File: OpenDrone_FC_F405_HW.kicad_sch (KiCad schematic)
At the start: 106 parts, among them J1 Conn_01x05, J10 Conn_01x02, J12 Conn_01x02, J13 Conn_01x02, J14 Conn_01x02, J15 Conn_01x02, J16 Conn_01x02, J17 Conn_01x02, J19 Conn_01x02, J2 Conn_01x02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

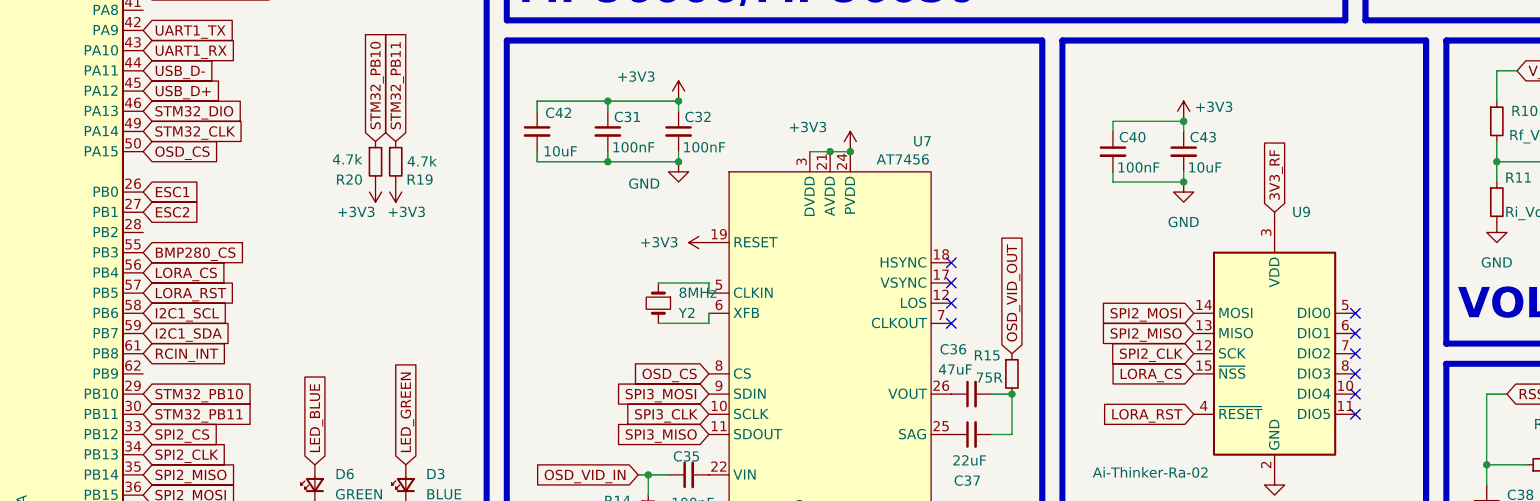
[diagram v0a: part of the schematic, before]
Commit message: add LoRa IRQ
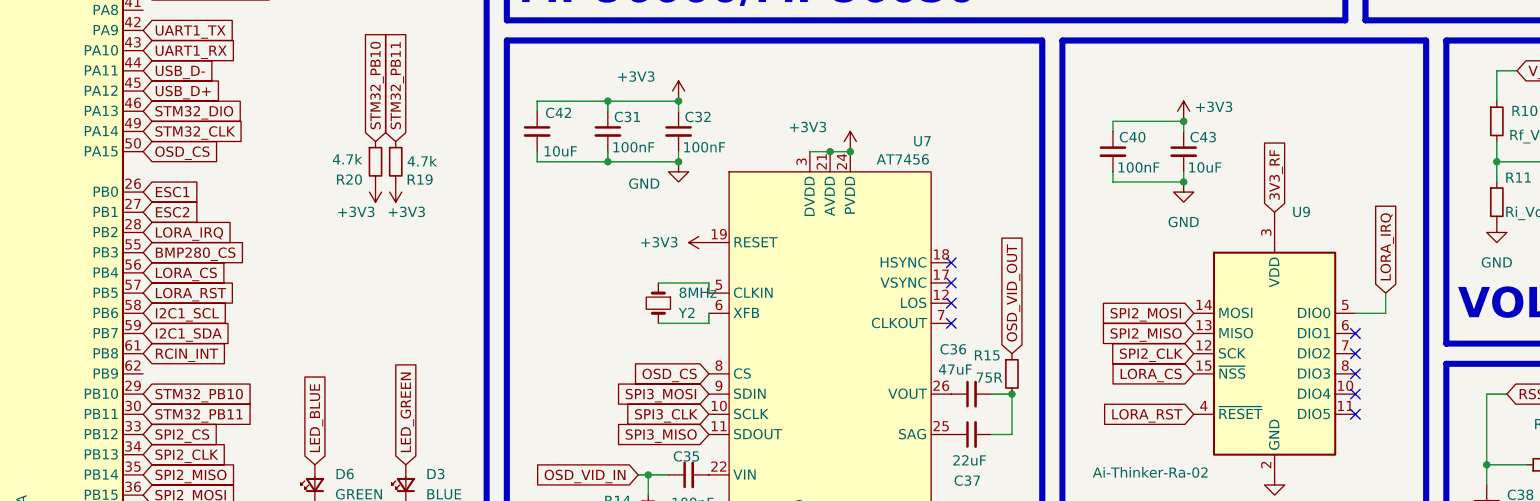
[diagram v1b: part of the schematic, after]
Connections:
- net LORA_IRQ: now reaches U9.5 (DIO0)
- net LORA_IRQ: now also U1.28 (PB2)
- no-connect marks 14 -> 13

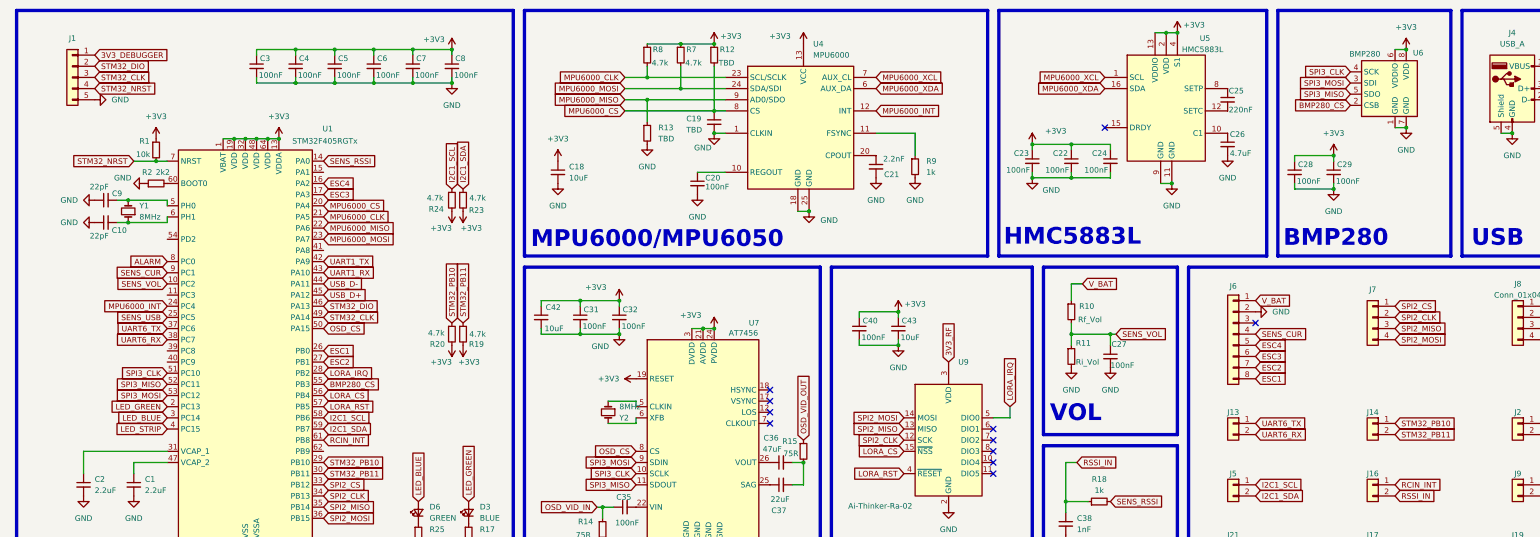
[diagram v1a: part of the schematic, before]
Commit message: use mpu6050 and change spi pinout
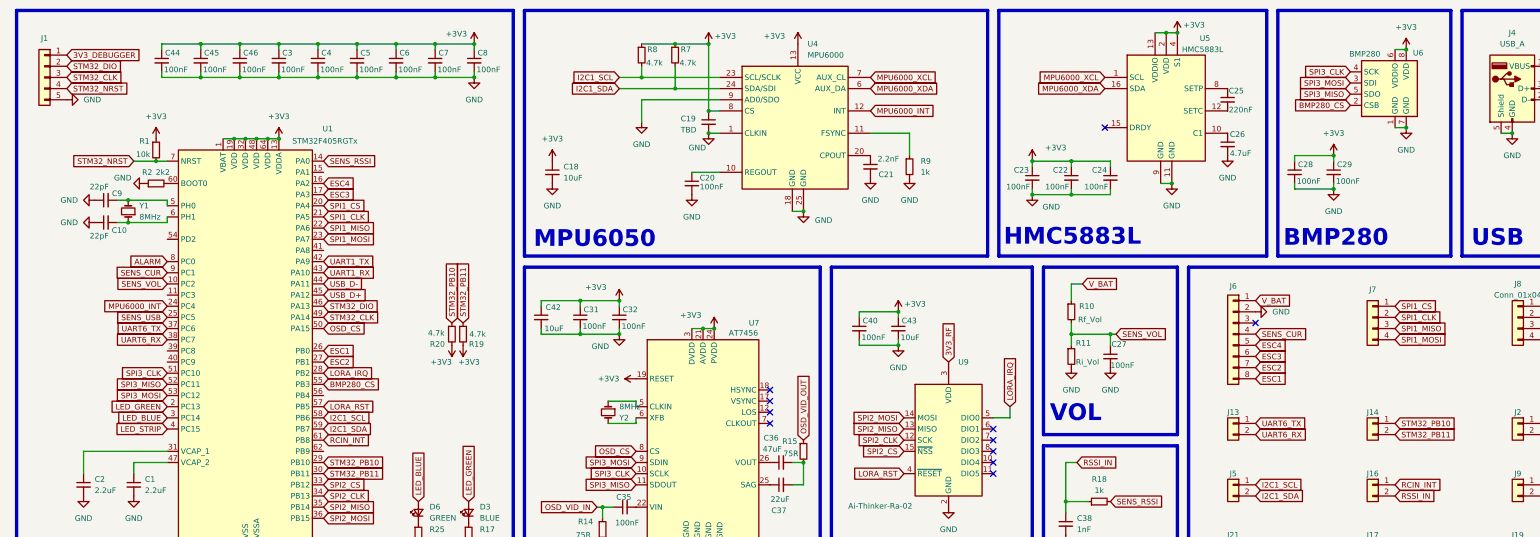
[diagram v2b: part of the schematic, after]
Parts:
- removed R12, R13: TBD, Capacitor_SMD:C_0402_1005Metric, symbol Device:R_Small
- removed R23, R24: 4.7k, Resistor_SMD:R_0402_1005Metric, symbol Device:R_Small
- added C44, C45, C46: 100nF, Capacitor_SMD:C_0402_1005Metric, symbol Device:C_Small
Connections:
- net +3V3: now also C19.1, U4.8 (CS), C44.1, C45.1, C46.1
- net GND: now also U4.9 (AD0/SDO), C44.2, C45.2, C46.2
- net I2C1_SCL: now also R8.2, U4.23 (SCL/SCLK)
- net I2C1_SDA: now also R7.2, U4.24 (SDA/SDI)
- net SPI2_CLK: no longer J7.2 (Pin_2)
- net SPI2_CS: now also U9.15 (~{NSS}); no longer J7.1 (Pin_1)
- net SPI2_MISO: no longer J7.3 (Pin_3)
- net SPI2_MOSI: no longer J7.4 (Pin_4)
- net LORA_CS: no longer names the net of U1.56 (PB4)
- net LORA_CS: no longer U9.15 (~{NSS})
- removed net MPU6000_CLK: R8.2, U1.21 (PA5), U4.23 (SCL/SCLK)
- removed net MPU6000_CS: C19.1, U1.20 (PA4), U4.8 (CS)
- net MPU6000_MISO renamed SPI1_MISO
- net SPI1_MISO: now also J7.3 (Pin_3); no longer U4.9 (AD0/SDO)
- removed net MPU6000_MOSI: R7.2, U1.23 (PA7), U4.24 (SDA/SDI)
- new net SPI1_CLK: J7.2 (Pin_2), U1.21 (PA5)
- new net SPI1_CS: J7.1 (Pin_1), U1.20 (PA4)
- new net SPI1_MOSI: J7.4 (Pin_4), U1.23 (PA7)
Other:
- note added: "MPU6050"
- note removed: "MPU6000/MPU6050"
- moved on the sheet: C18, C19, C20, C21, C22, C23, C24, C3, C4, C5, C6, C7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

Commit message: update project
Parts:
- removed C30, C34, C42: 10uF, Capacitor_SMD:C_1210_3225Metric, symbol Device:C_Small
- removed C31, C32, C35: 100nF, Capacitor_SMD:C_0402_1005Metric, symbol Device:C_Small
- removed C33, C40, C41: 100nF, Capacitor_SMD:C_1210_3225Metric, symbol Device:C_Small
- removed C36: 47uF, Capacitor_SMD:C_0402_1005Metric, symbol Device:C_Small
- removed C37: 22uF, Capacitor_SMD:C_0402_1005Metric, symbol Device:C_Small
- removed C38: 1nF, Capacitor_SMD:C_0402_1005Metric, symbol Device:C_Small
- removed C43: 10uF, Capacitor_SMD:C_0805_2012Metric, symbol Device:C_Small
- removed D5: SS34, Diode_SMD:D_SMA, symbol Device:D_Schottky
- removed J12, J15, J16, J17, J19, J20, J21: Conn_01x02, Footprint:MountingPad_1x2, symbol Connector_Generic:Conn_01x02
- removed J4: USB_A, Footprint:USB_Micro-B_SMD, symbol Connector:USB_A
- removed J7: Conn_01x04, Footprint:MountingPad_1x4, symbol Connector_Generic:Conn_01x04
- removed R14, R15: 75R, Resistor_SMD:R_0402_1005Metric, symbol Device:R_Small
- removed R18: 1k, Resistor_SMD:R_0402_1005Metric, symbol Device:R_Small
- removed R4, R6: 10k, Resistor_SMD:R_0402_1005Metric, symbol Device:R_Small
- removed U7: AT7456, Package_SO:TSSOP-28-1EP_4.4x9.7mm_P0.65mm, symbol AT7456:AT7456
- removed U9: Ai-Thinker-Ra-02, Footprint:Ai-Thinker-Ra-02-LoRa, symbol RF_Module:Ai-Thinker-Ra-02
- removed Y2: 8MHz, Crystal:Crystal_SMD_3225-4Pin_3.2x2.5mm, symbol Device:Crystal_Small
- added J11, J12, J16: Conn_01x05, Connector_PinHeader_2.00mm:PinHeader_1x05_P2.00mm_Vertical, symbol Connector_Generic:Conn_01x05
- added J3, J4, J7: Conn_01x02, Footprint:HolePad_1x2, symbol Connector_Generic:Conn_01x02
- C19: value TBD -> 10nF
- J13, J14, J2, J5, J9: footprint Footprint:MountingPad_1x2 -> Footprint:HolePad_1x2
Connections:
- net OSD_VID_IN is gone; now on net +5V: J2.1 (Pin_1)
- net OSD_VID_OUT is gone; now on net GND: J2.2 (Pin_2)
- net +3V3: now also J14.1 (Pin_1), J16.5 (Pin_5), J3.1 (Pin_1), J4.1 (Pin_1)
- net +5V: now also J13.1 (Pin_1), J16.3 (Pin_3)
- net ALARM: now also J9.2 (Pin_2); no longer J9.1 (Pin_1)
- net GND: now also J13.2 (Pin_2), J14.2 (Pin_2), J16.4 (Pin_4), J3.2 (Pin_2), J4.2 (Pin_2)
- net I2C1_SCL: now also U6.4 (SCK)
- net I2C1_SDA: now also U6.3 (SDI)
- net LED_STRIP: now also J9.1 (Pin_1); no longer J9.2 (Pin_2)
- net LORA_IRQ: now also J12.5 (Pin_5)
- net LORA_RST: now also J11.5 (Pin_5)
- net OSD_CS: no longer U1.50 (PA15)
- net SPI1_CLK: now also J11.2 (Pin_2)
- net SPI1_CS: now also J11.1 (Pin_1)
- net SPI1_MISO: now also J11.3 (Pin_3)
- net SPI1_MOSI: now also J11.4 (Pin_4)
- net SPI2_CLK: now also J12.2 (Pin_2)
- net SPI2_CS: now also J12.1 (Pin_1)
- net SPI2_MISO: now also J12.3 (Pin_3)
- net SPI2_MOSI: now also J12.4 (Pin_4)
- net STM32_PB10: now also J16.1 (Pin_1); no longer J14.1 (Pin_1)
- net STM32_PB11: now also J16.2 (Pin_2); no longer J14.2 (Pin_2)
- net UART6_RX: now also J7.2 (Pin_2); no longer J13.2 (Pin_2)
- net UART6_TX: now also J7.1 (Pin_1); no longer J13.1 (Pin_1)
- net BMP280_CS: no longer names the net of U6.2 (CSB)
- net BMP280_CS: no longer U1.55 (PB3)
- net RCIN_INT: no longer names the net of U1.61 (PB8)
- net SENS_RSSI: no longer names the net of U1.14 (PA0)
- net SENS_USB: no longer names the net of U1.25 (PC5)
- net SPI3_CLK: no longer names the net of U1.51 (PC10)
- net SPI3_CLK: no longer U6.4 (SCK)
- net SPI3_MISO: no longer names the net of U6.5 (SDO)
- net SPI3_MISO: no longer U1.52 (PC11)
- net SPI3_MOSI: no longer names the net of U1.53 (PC12)
- net SPI3_MOSI: no longer U6.3 (SDI)
- net USB_D+: no longer names the net of U1.45 (PA12)
- net USB_D-: no longer names the net of U1.44 (PA11)
- no-connect marks 13 -> 6
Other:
- note removed: "LORA"
- note removed: "OSD"
- note removed: "RSSI"
- note removed: "USB"
- moved on the sheet: C14, C15, C16, C17, C27, C28, C29, C39, D2, D3, D4, D6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

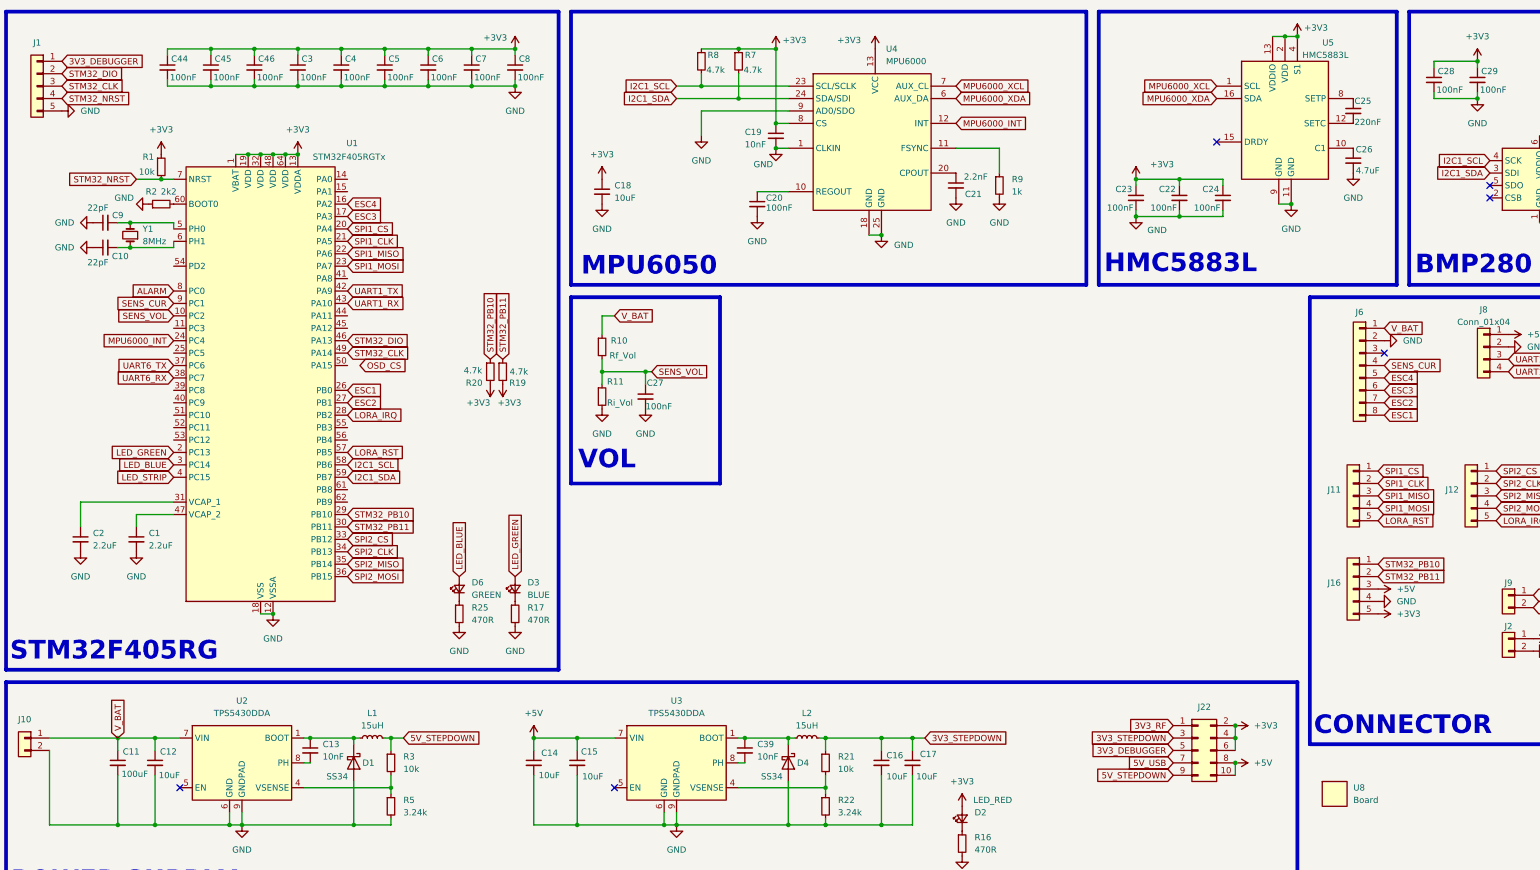
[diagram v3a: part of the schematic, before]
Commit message: update placement
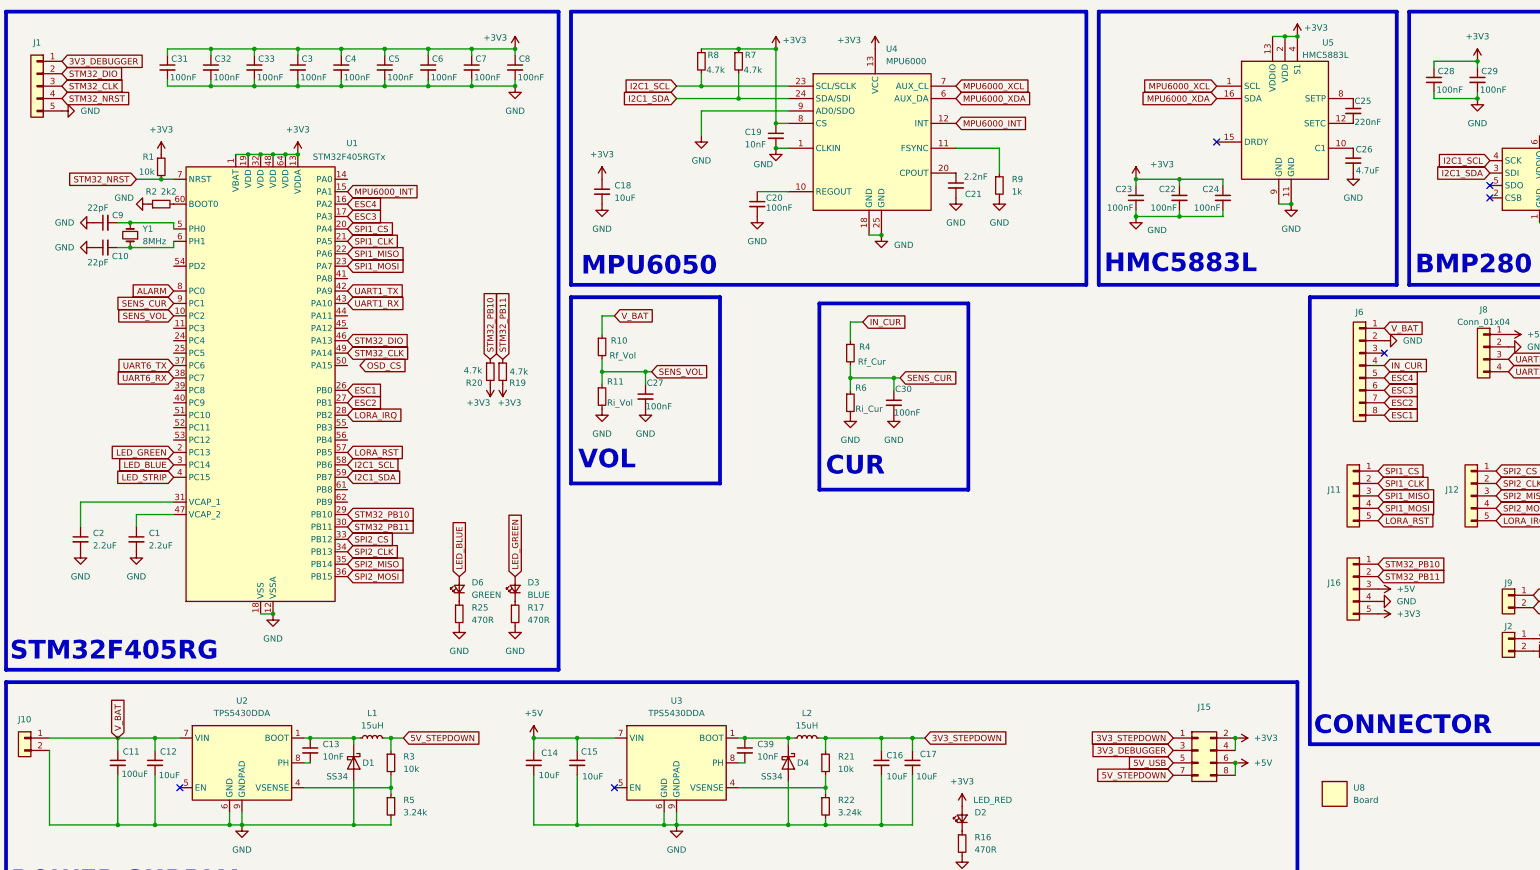
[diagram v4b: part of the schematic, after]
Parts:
- removed C44, C45, C46: 100nF, Capacitor_SMD:C_0402_1005Metric, symbol Device:C_Small
- removed J22: Conn_02x05_Odd_Even, Connector_PinHeader_1.27mm:PinHeader_2x05_P1.27mm_Vertical, symbol Connector_Generic:Conn_02x05_Odd_Even
- added C30, C31, C32, C33: 100nF, Capacitor_SMD:C_0402_1005Metric, symbol Device:C_Small
- added J15: Conn_02x04_Odd_Even, Connector_PinHeader_1.27mm:PinHeader_2x04_P1.27mm_Vertical, symbol Connector_Generic:Conn_02x04_Odd_Even
- added R4: Rf_Cur, Resistor_SMD:R_0402_1005Metric, symbol Device:R_Small
- added R6: Ri_Cur, Resistor_SMD:R_0402_1005Metric, symbol Device:R_Small
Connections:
- net +3V3: now also C31.1, C32.1, C33.1, J15.2 (Pin_2), J15.4 (Pin_4)
- net +5V: now also J15.6 (Pin_6), J15.8 (Pin_8)
- net 3V3_DEBUGGER: now also J15.3 (Pin_3)
- net 3V3_STEPDOWN: now also J15.1 (Pin_1)
- net 5V_STEPDOWN: now also J15.7 (Pin_7)
- net 5V_USB: now also J15.5 (Pin_5)
- net GND: now also C30.2, C31.2, C32.2, C33.2, R6.2
- net MPU6000_INT: now also U1.15 (PA1); no longer U1.24 (PC4)
- net SENS_CUR: now also C30.1, R4.2, R6.1; no longer J6.4 (Pin_4)
- new net IN_CUR: J6.4 (Pin_4), R4.1
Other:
- note added: "CUR"

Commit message: update project
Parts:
- removed J15: Conn_02x04_Odd_Even, Connector_PinHeader_1.27mm:PinHeader_2x04_P1.27mm_Vertical, symbol Connector_Generic:Conn_02x04_Odd_Even
- added J17: Conn_02x03_Odd_Even, Connector_PinHeader_1.27mm:PinHeader_2x03_P1.27mm_Vertical, symbol Connector_Generic:Conn_02x03_Odd_Even
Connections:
- net +3V3: now also J17.2 (Pin_2), J17.4 (Pin_4)
- net +5V: now also J17.5 (Pin_5)
- net 3V3_DEBUGGER: now also J17.3 (Pin_3)
- net 3V3_STEPDOWN: now also J17.1 (Pin_1)
- net 5V_STEPDOWN: now also J17.6 (Pin_6)
- net LORA_IRQ: now also J11.1 (Pin_1), U1.45 (PA12); no longer J12.5 (Pin_5), U1.28 (PB2)
- net LORA_RST: now also J12.1 (Pin_1), U1.44 (PA11); no longer J11.5 (Pin_5), U1.57 (PB5)
- net SPI1_CLK: no longer J11.2 (Pin_2)
- net SPI1_CS: no longer J11.1 (Pin_1)
- net SPI1_MISO: no longer J11.3 (Pin_3)
- net SPI1_MOSI: no longer J11.4 (Pin_4)
- net SPI2_CLK: now also J11.4 (Pin_4); no longer J12.2 (Pin_2)
- net SPI2_CS: now also J11.5 (Pin_5); no longer J12.1 (Pin_1)
- net SPI2_MISO: now also J11.3 (Pin_3); no longer J12.3 (Pin_3)
- net SPI2_MOSI: now also J11.2 (Pin_2); no longer J12.4 (Pin_4)
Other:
- moved on the sheet: J13, J14, J16, J2, J4, J7, J9
